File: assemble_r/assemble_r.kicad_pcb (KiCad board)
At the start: 2 copper layers, 128.5 x 92.1 mm, 45 parts, among them J23 Conn_01x02_Pin, SW23 SW_Push, SW24 SW_Push, SW25 SW_Push, SW26 SW_Push, SW27 SW_Push, SW28 SW_Push, SW29 SW_Push, SW30 SW_Push, SW31 SW_Push, SW32 SW_Push, SW33 SW_Push, SW34 SW_Push, SW35 SW_Push, SW36 SW_Push, SW37 SW_Push, SW38 SW_Push, SW39 SW_Push, SW40 SW_Push, SW41 SW_Push, SW42 SW_Push, SW43 SW_Push, SW44 SW_Push, U23 Micon_BLEMicroPro

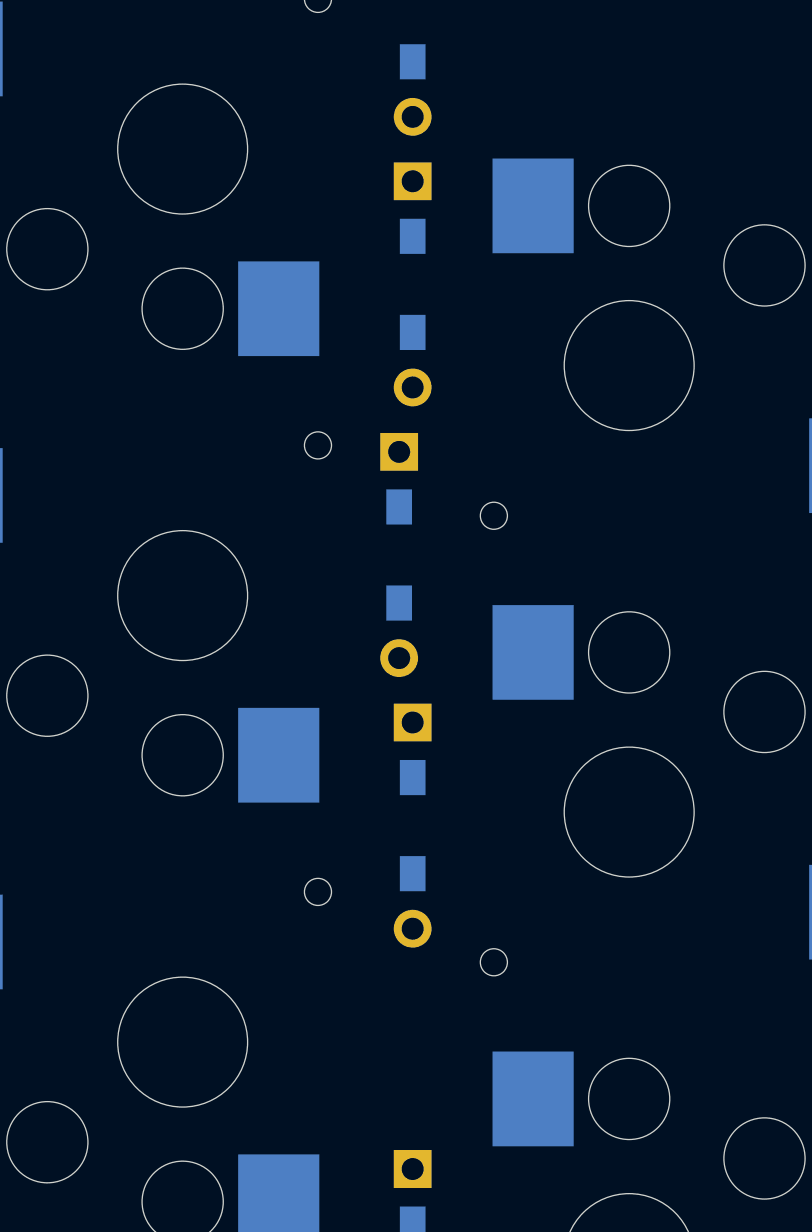
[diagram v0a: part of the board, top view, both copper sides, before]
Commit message: fix: some diode place
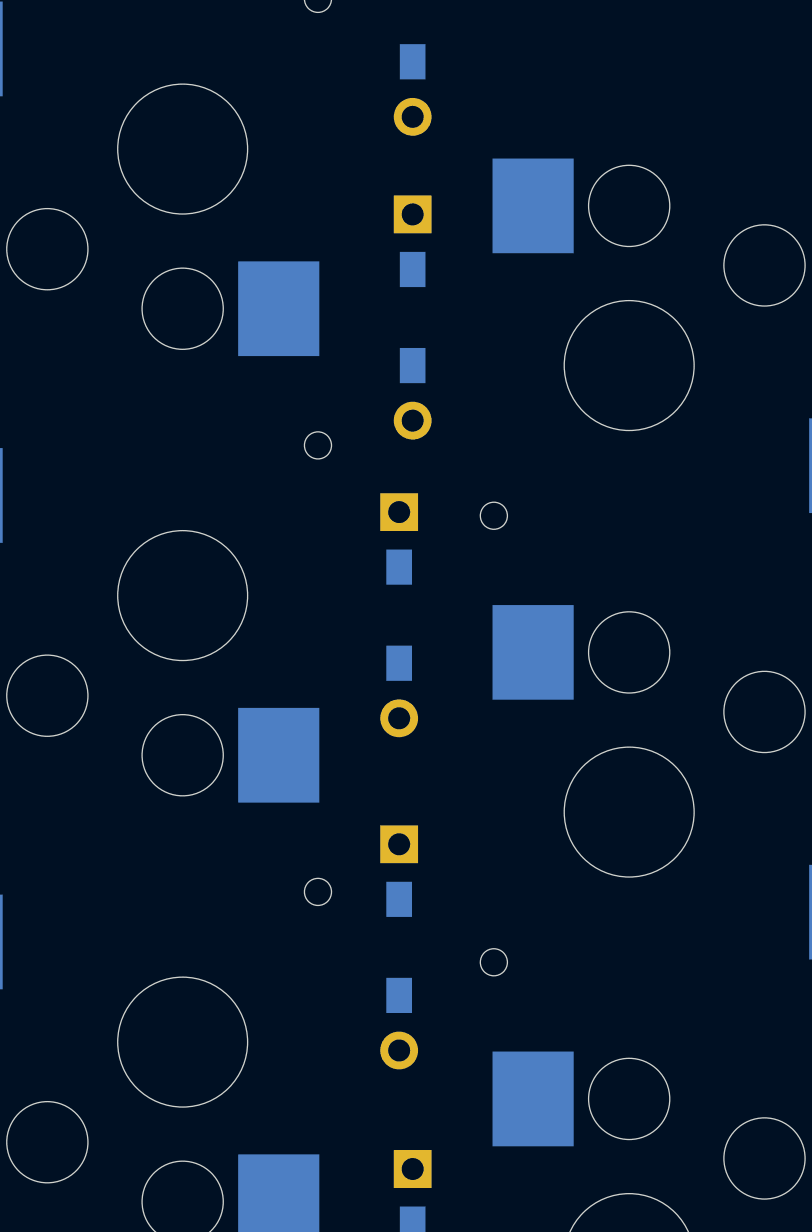
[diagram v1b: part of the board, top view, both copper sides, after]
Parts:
- moved D40 4.53 mm to (128.5, 72.5)
- moved D36 2.23 mm to (128.5, 60.2)
- moved D39 1.23 mm to (129.0, 49.2)
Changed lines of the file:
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@@
 		(fp_line
 			(start -7.305 2.375)
-			(end -7.304999 5.025)
+			(end -7.304998 5.025)
 			(stroke
 				(width 0.15)
@@
 		(fp_line
 			(start 0.5 8.2)
-			(end 0.5 3.599999)
+			(end 0.5 3.599998)
 			(stroke
 				(width 0.15)
@@
 			(start -6.305 6.025)
 			(mid -7.012107 5.732107)
-			(end -7.304999 5.025)
+			(end -7.304998 5.025)
 			(stroke
 				(width 0.15)
@@
 		(fp_arc
 			(start -1.275 3.575)
-			(mid -2.10585 3.230851)
+			(mid -2.10585 3.230852)
 			(end -2.450001 2.4)
 			(stroke
@@
 		)
 		(pad "" np_thru_hole circle
-			(at 5 -5.550001 15)
+			(at 5 -5.550002 15)
 			(size 1 1)
 			(drill oval 1)
@@
 	(footprint "kbd_Parts:Diode_TH_SMD"
 		(layer "F.Cu")
-		(at 129 68 -90)
+		(at 128.5 72.5 -90)
 		(descr "Resitance 3 pas")
 		(tags "R")
@@
 	(footprint "kbd_Parts:Diode_TH_SMD"
 		(layer "F.Cu")
-		(at 129 48 -90)
+		(at 129 49.225 -90)
 		(descr "Resitance 3 pas")
 		(tags "R")
@@
 		)
 		(fp_line
-			(start -0.850001 8.2)
+			(start -0.850002 8.2)
 			(end -0.85 3.6)
 			(stroke
@@
 		(fp_line
 			(start 0.65 8.2)
-			(end 0.649999 3.6)
+			(end 0.649998 3.6)
 			(stroke
 				(width 0.15)
@@
 		)
 		(fp_arc
-			(start -6.305 6.024999)
+			(start -6.305 6.024998)
 			(mid -7.012107 5.732107)
 			(end -7.305 5.025)
@@
 	(footprint "kbd_Parts:Diode_TH_SMD"
 		(layer "F.Cu")
-		(at 128.5 58 -90)
+		(at 128.5 60.225 -90)
 		(descr "Resitance 3 pas")
 		(tags "R")
@@
 		)
 		(fp_line
-			(start -4.6 6.000001)
+			(start -4.6 6.000002)
 			(end -4.6 1.4)
 			(stroke
@@
 		)
 		(fp_line
-			(start -1.3 7.989999)
+			(start -1.3 7.989998)
 			(end -1.3 3.6)
 			(stroke
@@
 		(fp_line
 			(start -0.4 8.2)
-			(end -0.399999 3.6)
+			(end -0.399998 3.6)
 			(stroke
 				(width 0.15)
@@
 		)
 		(fp_line
-			(start 1.85 7.660001)
+			(start 1.85 7.660002)
 			(end 1.85 4.13)
 			(stroke
@@
 		)
 		(pad "" np_thru_hole circle
-			(at 5.000001 -5.55 2.5)
+			(at 5.000002 -5.55 2.5)
 			(size 1 1)
 			(drill oval 1)

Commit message: fix: re-change layout
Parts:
- moved D38 45.8 mm to (133.0, 46.5)
- moved SW38 44.5 mm to (137.0, 51.2)
- moved D41 36.9 mm to (161.5, 56.0)
- moved SW41 36.9 mm to (153.5, 51.0), turned to 0 degrees
- moved D43 16.5 mm to (161.0, 83.0)
- moved SW42 16.5 mm to (153.5, 67.5)
- moved SW43 16.5 mm to (153.5, 84.0)
- moved D42 16.5 mm to (161.0, 67.7)
- moved SW39 16.5 mm to (137.0, 67.5), turned to 0 degrees
- moved SW40 16.5 mm to (137.0, 84.0), turned to 0 degrees
- moved D39 15.1 mm to (130.0, 64.3)
- moved D40 13.5 mm to (129.0, 86.0)
- moved D37 11.0 mm to (124.5, 74.5)
- moved D36 5.63 mm to (123.0, 59.0)
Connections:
- D38 pad 1: Row3 -> Row2
- SW38 pad 1: Col3 -> Col5
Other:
- outline, holes or cut-outs redrawn

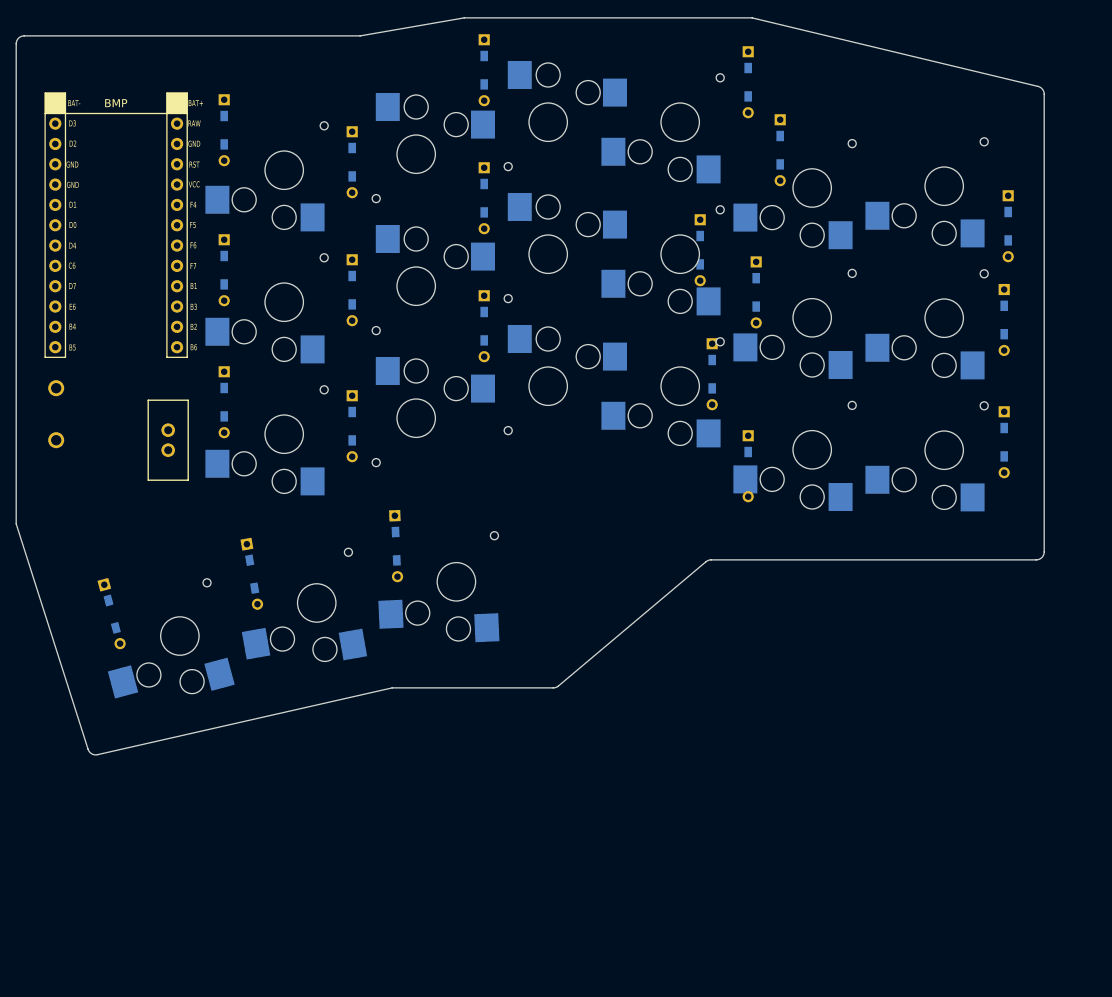
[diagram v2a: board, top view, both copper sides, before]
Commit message: fix: change outline
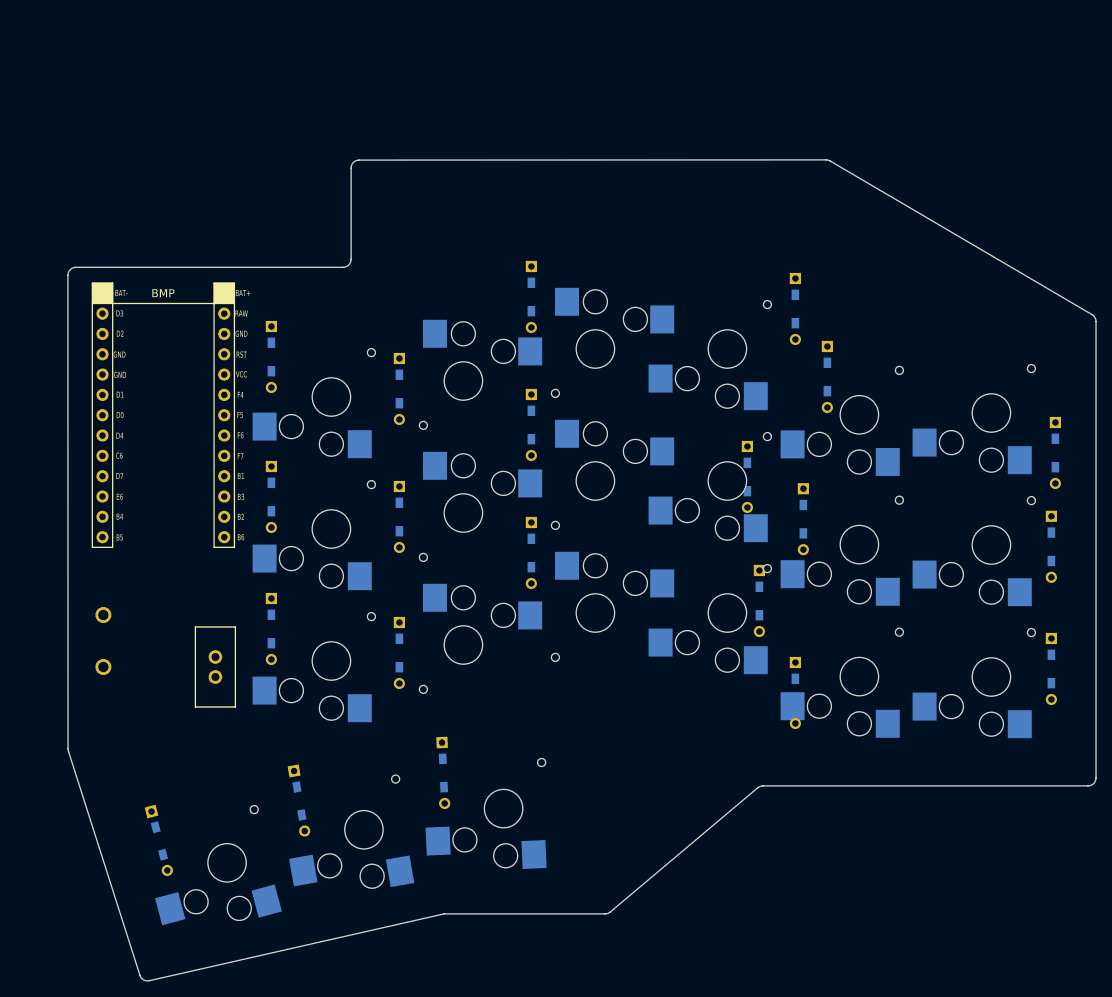
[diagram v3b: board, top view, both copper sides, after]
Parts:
- moved D42 29.0 mm to (166.9, 96.1)
- moved SW34 29.0 mm to (98.4, 128.8)
- moved SW30 29.0 mm to (81.0, 131.4)
- moved SW38 29.0 mm to (142.9, 79.6)
- moved D23 29.0 mm to (69.4, 72.3)
- moved D24 29.0 mm to (69.4, 89.8)
- moved D25 29.0 mm to (69.4, 106.3)
- moved D26 29.0 mm to (55.4, 132.8)
- moved D27 29.0 mm to (85.4, 76.3)
- moved D28 29.0 mm to (85.4, 92.3)
- moved D29 29.0 mm to (85.4, 109.3)
- moved D30 29.0 mm to (72.9, 127.8)
- moved D31 29.0 mm to (101.9, 64.8)
- moved D32 29.0 mm to (101.9, 80.8)
- moved D33 29.0 mm to (101.9, 96.8)
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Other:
- board size 128.5 x 92.1 mm -> 128.5 x 102.6 mm

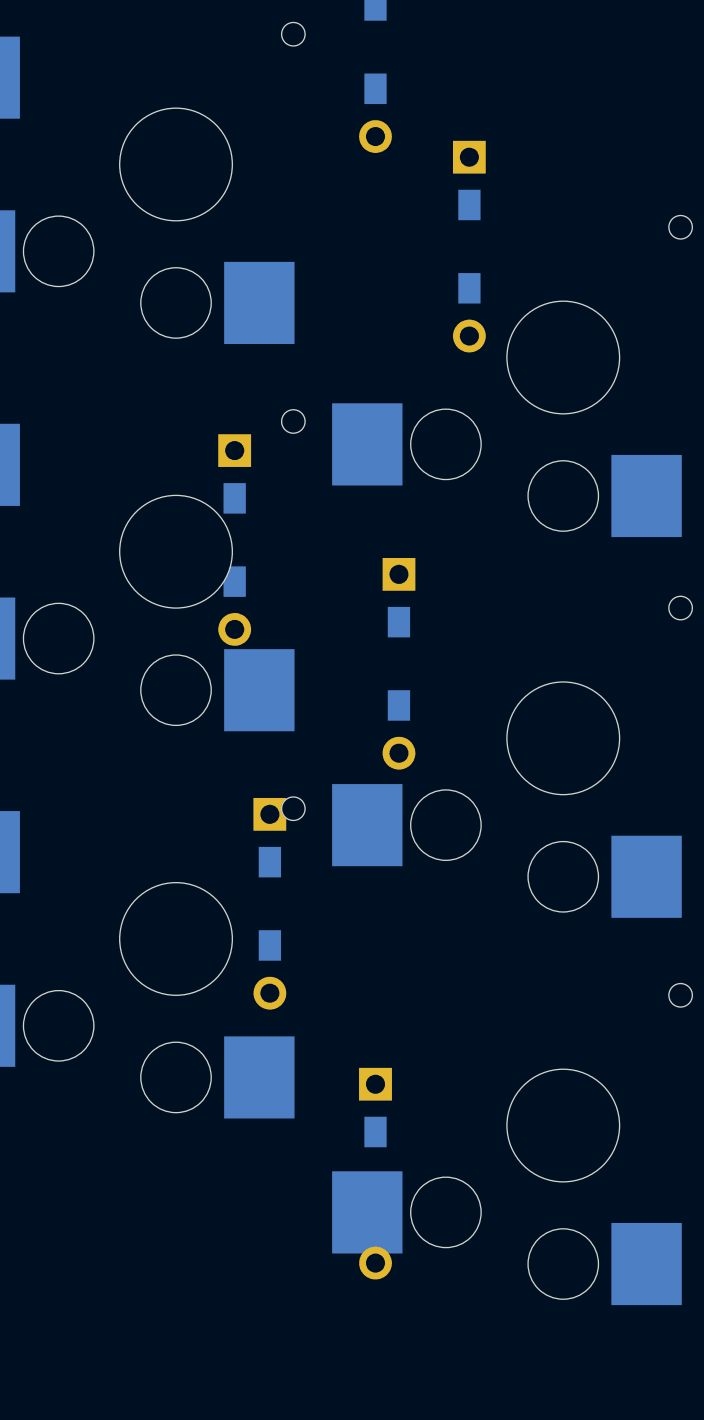
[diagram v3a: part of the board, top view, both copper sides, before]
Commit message: fix: DRC error
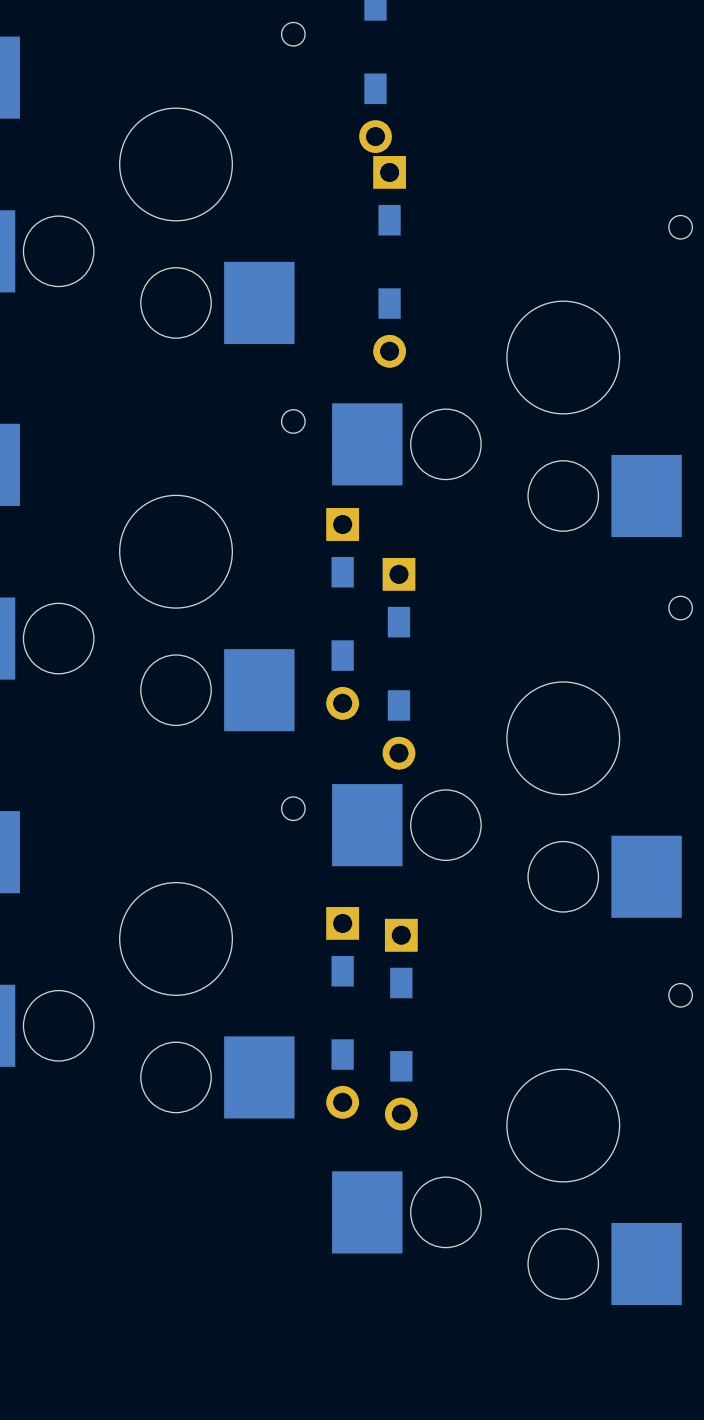
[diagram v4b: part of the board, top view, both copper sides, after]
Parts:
- moved D40 6.44 mm to (136.0, 108.0)
- moved D37 5.59 mm to (133.5, 107.5)
- moved D36 5.58 mm to (133.5, 90.5)
- moved D38 3.46 mm to (135.5, 75.5)
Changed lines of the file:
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@@
 	(footprint "kbd_Parts:Diode_TH_SMD"
 		(layer "F.Cu")
-		(at 130.4 102.85 -90)
+		(at 133.5 107.5 -90)
 		(descr "Resitance 3 pas")
 		(tags "R")
@@
 	(footprint "kbd_Parts:Diode_TH_SMD"
 		(layer "F.Cu")
-		(at 134.9 114.35 -90)
+		(at 136 108 -90)
 		(descr "Resitance 3 pas")
 		(tags "R")
@@
 	(footprint "kbd_Parts:Diode_TH_SMD"
 		(layer "F.Cu")
-		(at 138.9 74.85 -90)
+		(at 135.5 75.5 -90)
 		(descr "Resitance 3 pas")
 		(tags "R")
@@
 	(footprint "kbd_Parts:Diode_TH_SMD"
 		(layer "F.Cu")
-		(at 128.9 87.35 -90)
+		(at 133.5 90.5 -90)
 		(descr "Resitance 3 pas")
 		(tags "R")
@@
 		)
 		(fp_line
-			(start -4.6 6.000004)
+			(start -4.6 6.000005)
 			(end -4.6 1.4)
 			(stroke
@@
 		(fp_line
 			(start -0.4 8.2)
-			(end -0.399996 3.6)
+			(end -0.399995 3.6)
 			(stroke
 				(width 0.15)
@@
 		)
 		(pad "" np_thru_hole circle
-			(at 5.000004 -5.55 2.5)
+			(at 5.000005 -5.55 2.5)
 			(size 1 1)
 			(drill oval 1)
@@
 		(layer "Edge.Cuts")
 	)
-	(gr_line
-		(start 43.965651 61.1375)
-		(end 43.965651 61.1375)
-		(stroke
-			(width 0.05)
-			(type default)
-		)
-		(layer "Edge.Cuts")
-	)
 	(gr_arc
 		(start 44.025412 121.610664)
@@
 		(stroke
 			(width 0.05)
-			(type default)
-		)
-		(layer "Edge.Cuts")
-	)
-	(gr_line
-		(start 43.965651 61.1375)
-		(end 43.965651 61.1375)
-		(stroke
-			(width 0.05)

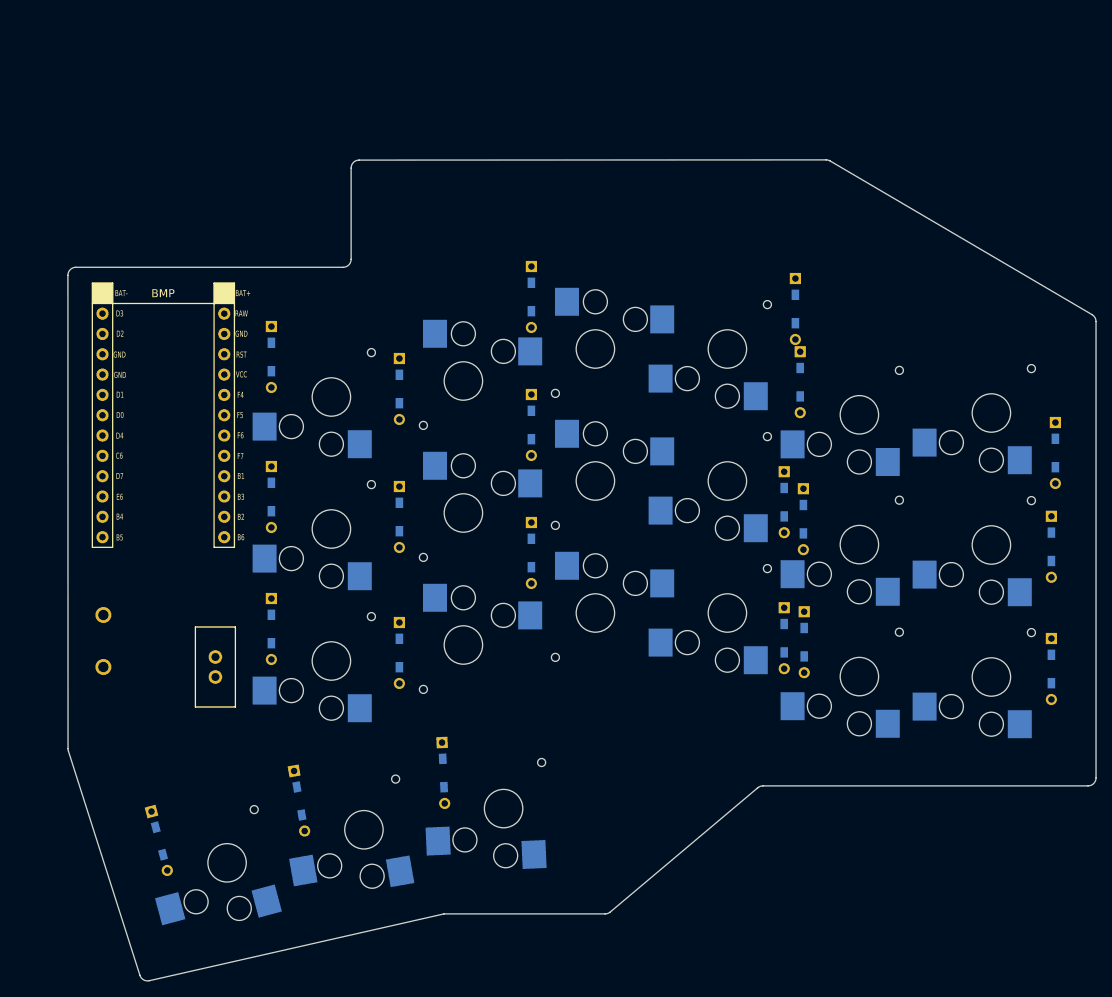
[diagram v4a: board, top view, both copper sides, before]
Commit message: feat: add screw
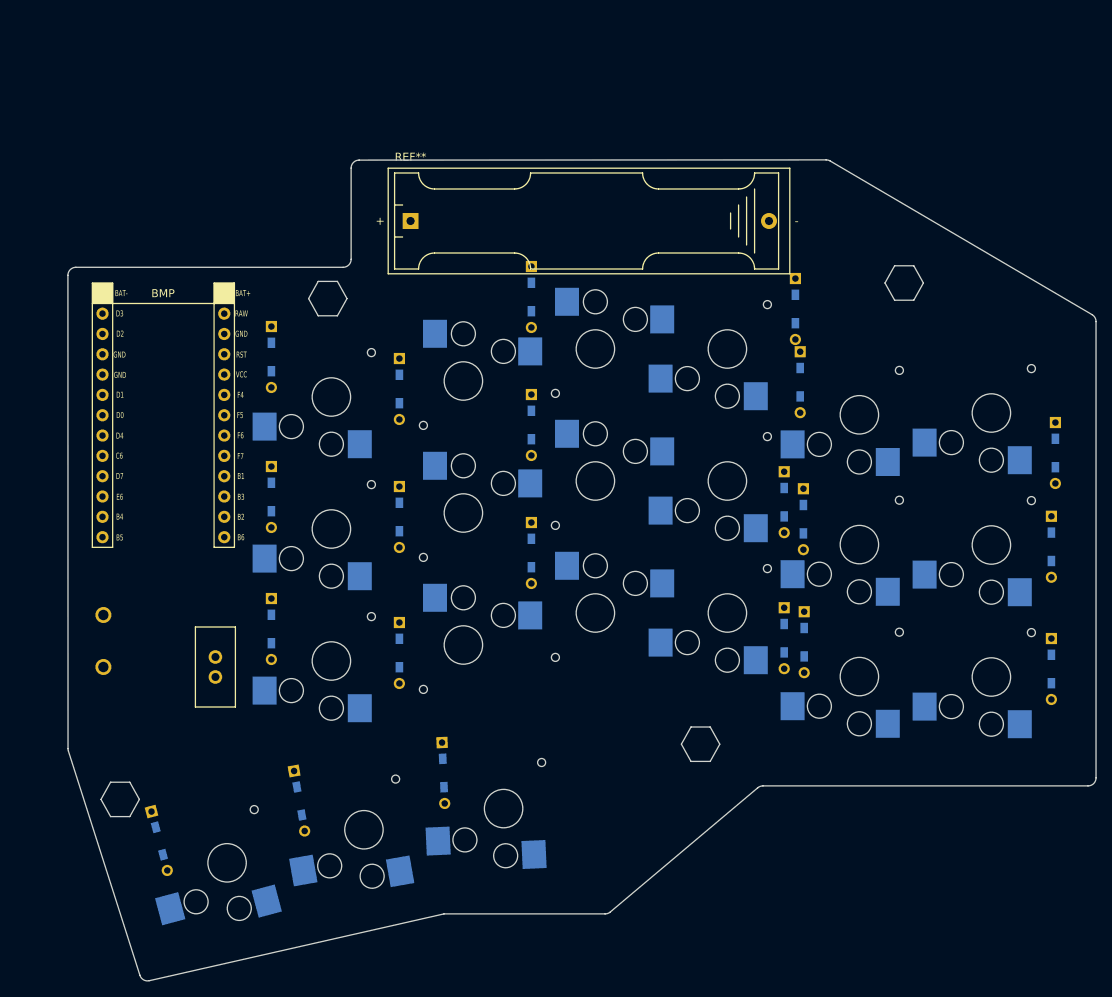
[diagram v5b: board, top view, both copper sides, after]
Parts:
- added REF**: BatteryHolder_単4, kbd_Parts:Battery_AAA, F.Cu at (86.8, 55.4)
- added Ref**: Val**, kbd_Hole:m2_Spacer_Hole_hex, F.Cu at (148.5, 63.1)
- added Ref**: Val**, kbd_Hole:m2_Spacer_Hole_hex, F.Cu at (76.5, 65.0)
- added Ref**: Val**, kbd_Hole:m2_Spacer_Hole_hex, F.Cu at (50.5, 127.7)
- added Ref**: Val**, kbd_Hole:m2_Spacer_Hole_hex, F.Cu at (123.0, 120.8)
